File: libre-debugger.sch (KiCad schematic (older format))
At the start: 81 parts, among them J1 USB_C_Receptacle_USB2.0, J2 Conn_ST_STDC14, J4 Conn_01x16, Q1 2N7002, SW1 SW_SPDT, SW2 SW_Push, U1 FT2232H, U10 74LVC1G125, U11 74LVC1G125, U12 74LVC1G125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

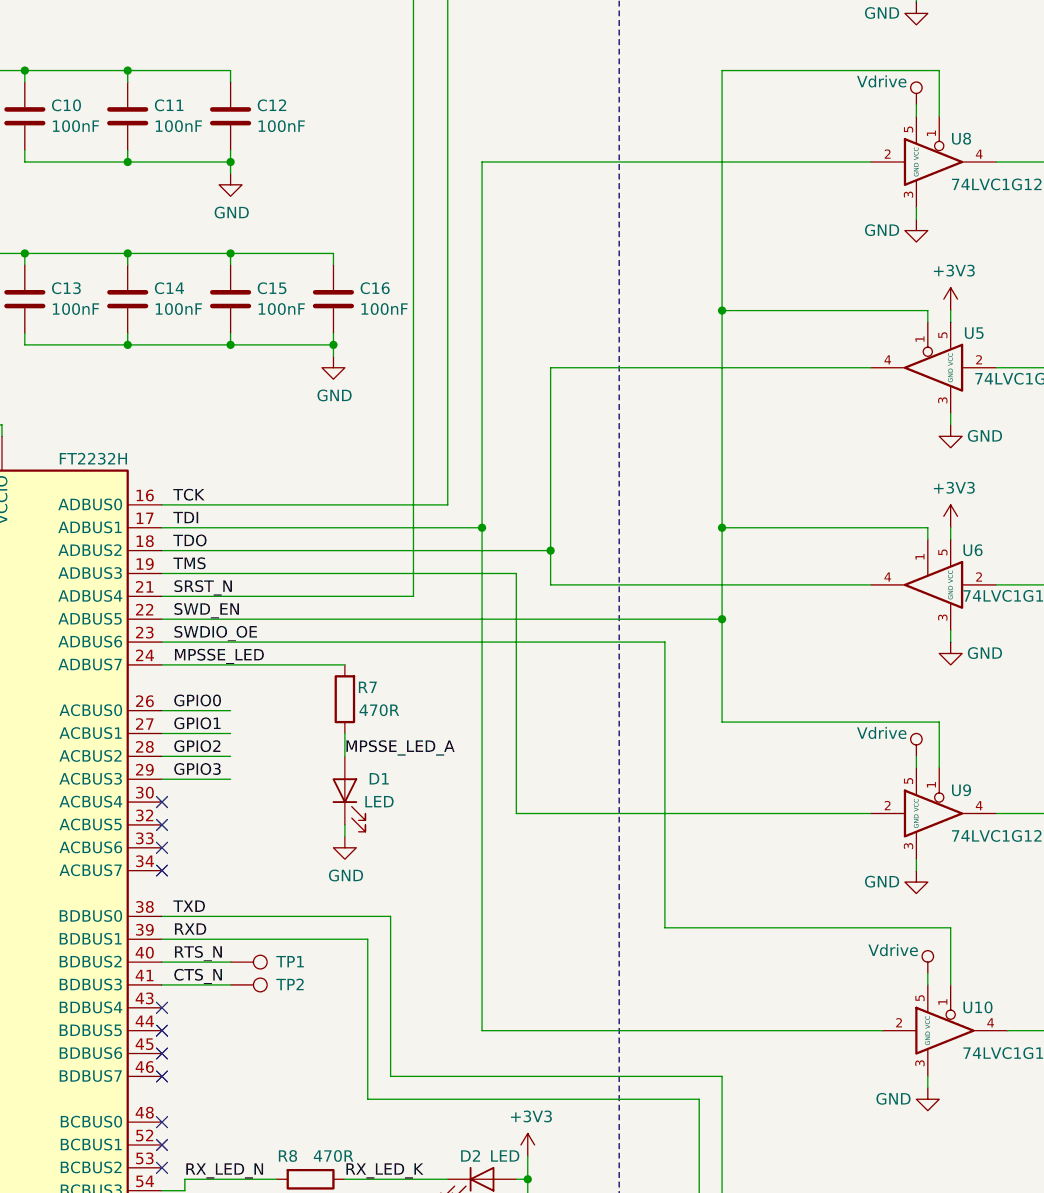
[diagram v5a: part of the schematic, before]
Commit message: Make MPSSE LED active low
So that all the activity LEDs have the same orientation.
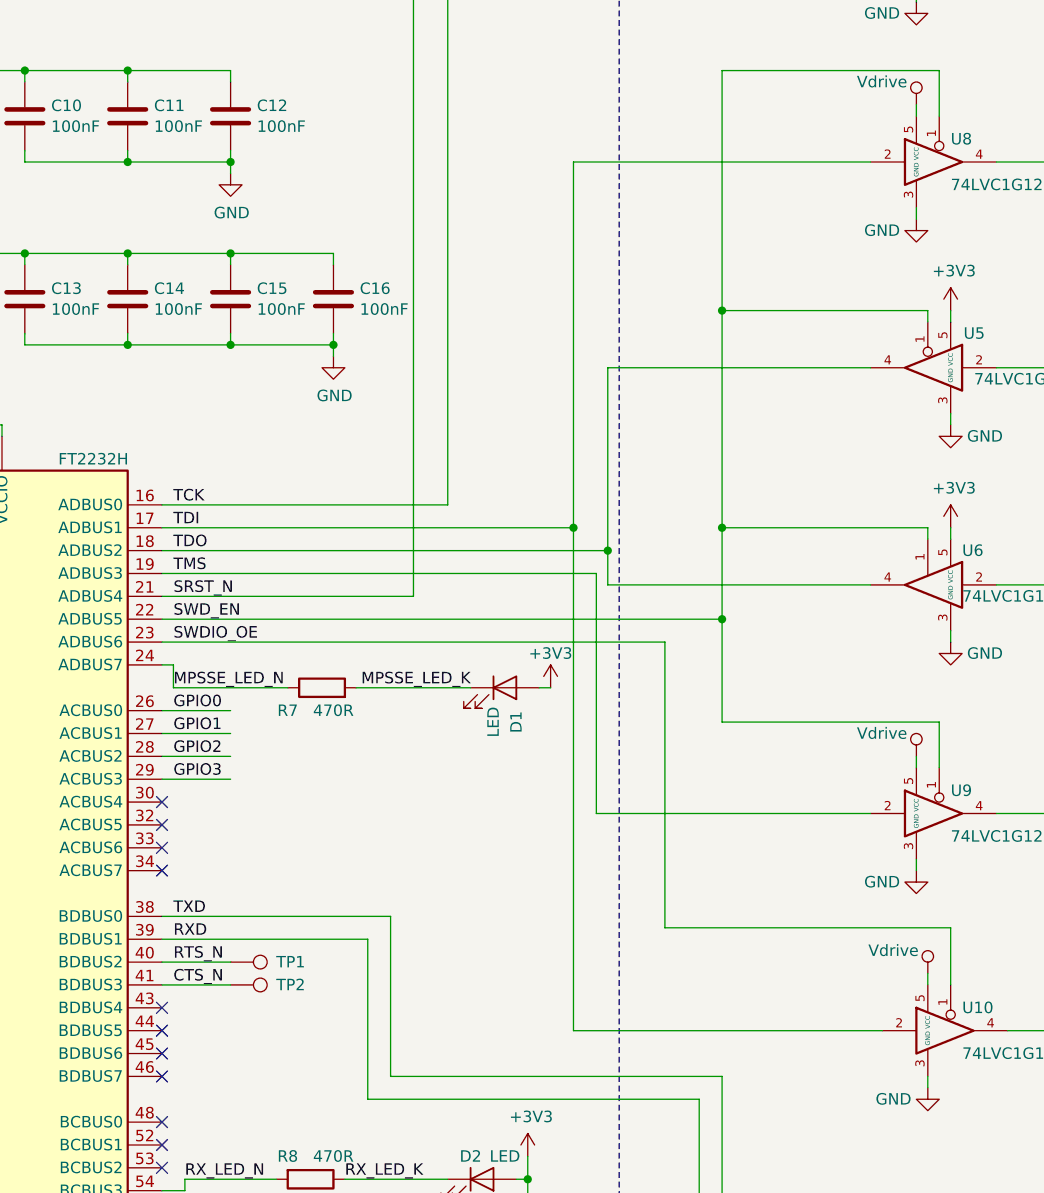
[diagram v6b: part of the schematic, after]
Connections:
- net labels added: MPSSE_LED_K, MPSSE_LED_N
- net labels removed: MPSSE_LED, MPSSE_LED_A
- wire segments 367 -> 369
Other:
- moved on the sheet: D1, R7
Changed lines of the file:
@@
 Text Notes 8850 7850 0    50   ~ 0
 ON only when USB configured
-Text Label 8450 4750 0    50   ~ 0
-MPSSE_LED
-$Comp
-L Device:LED D1
-U 1 1 5C62F385
-P 9200 5300
-F 0 "D1" V 9250 5150 50  0000 C CNN
-F 1 "LED" V 9150 5150 50  0000 C CNN
-F 2 "LED_SMD:LED_0603_1608Metric" H 9200 5300 50  0001 C CNN
-F 3 "~" H 9200 5300 50  0001 C CNN
-	1    9200 5300
-	0    -1   -1   0
-$EndComp
-Text Label 9200 5150 0    50   ~ 0
-MPSSE_LED_A
-Wire Wire Line
-	8400 4750 9200 4750
-$Comp
-L power:GND #PWR031
-U 1 1 5C6507DD
-P 9200 5500
-F 0 "#PWR031" H 9200 5250 50  0001 C CNN
-F 1 "GND" H 9205 5327 50  0000 C CNN
-F 2 "" H 9200 5500 50  0001 C CNN
-F 3 "" H 9200 5500 50  0001 C CNN
-	1    9200 5500
-	1    0    0    -1
-$EndComp
 Wire Wire Line
 	9650 4050 9650 1600
@@
 SWDIO_OE
 Wire Wire Line
-	8400 4150 9800 4150
-Wire Wire Line
-	9800 2550 9800 4150
+	8400 4150 10200 4150
+Wire Wire Line
+	10200 2550 10200 4150
 Wire Wire Line
 	9300 5950 9300 6650
@@
 Wire Wire Line
 	8400 4550 10850 4550
-$Comp
-L Device:R R7
-U 1 1 5C62F38F
-P 9200 4900
-F 0 "R7" H 9100 4850 50  0000 C CNN
-F 1 "470R" H 9050 4950 50  0000 C CNN
-F 2 "Resistor_SMD:R_0603_1608Metric" V 9130 4900 50  0001 C CNN
-F 3 "~" H 9200 4900 50  0001 C CNN
-	1    9200 4900
-	-1   0    0    1
-$EndComp
-Wire Wire Line
-	9200 5500 9200 5450
-Wire Wire Line
-	9200 5150 9200 5050
-Wire Wire Line
-	8400 4350 9950 4350
-Connection ~ 9800 4150
+Wire Wire Line
+	8400 4350 10300 4350
+Connection ~ 10200 4150
 Wire Wire Line
 	8400 4650 10600 4650
@@
 	9650 1600 11500 1600
 Wire Wire Line
-	9800 2550 11500 2550
+	10200 2550 11500 2550
 Wire Wire Line
 	11800 2150 10850 2150
@@
 $EndComp
 Wire Wire Line
-	11500 4400 10100 4400
-Wire Wire Line
-	10100 4400 10100 4250
-Wire Wire Line
 	13750 3000 13750 3450
 Wire Wire Line
@@
 	13650 4400 13650 2900
 Wire Wire Line
-	9950 5400 11500 5400
-Wire Wire Line
-	9950 4350 9950 5400
+	10300 5400 11500 5400
+Wire Wire Line
+	10300 4350 10300 5400
 Wire Wire Line
 	12050 5400 13650 5400
@@
 Connection ~ 13650 5400
 Wire Wire Line
-	9800 4150 9800 6350
+	10200 4150 10200 6350
 Wire Wire Line
 	10850 2150 10850 3200
@@
 	9400 5850 9400 6550
 Wire Wire Line
-	9800 6350 11550 6350
+	10200 6350 11550 6350
 Wire Wire Line
 	10600 4650 10600 5900
 Wire Wire Line
-	10100 3450 11500 3450
-Connection ~ 10100 4250
-Wire Wire Line
-	8400 4250 10100 4250
-Wire Wire Line
-	10100 3450 10100 4250
+	10350 3450 11500 3450
 Wire Notes Line
 	10400 600  13350 600
@@
 Wire Wire Line
 	5300 4650 5300 4600
+Wire Wire Line
+	10350 3450 10350 4250
+Wire Wire Line
+	8400 4250 10350 4250
+Connection ~ 10350 4250
+Wire Wire Line
+	10350 4400 10350 4250
+Wire Wire Line
+	11500 4400 10350 4400
+Text Label 8450 4850 0    50   ~ 0
+MPSSE_LED_N
+Wire Wire Line
+	8400 4750 8450 4750
+Wire Wire Line
+	8450 4850 8450 4750
+$Comp
+L Device:R R7
+U 1 1 5C62F38F
+P 9100 4850
+F 0 "R7" V 9000 5000 50  0000 C CNN
+F 1 "470R" V 9000 4800 50  0000 C CNN
+F 2 "Resistor_SMD:R_0603_1608Metric" V 9030 4850 50  0001 C CNN
+F 3 "~" H 9100 4850 50  0001 C CNN
+	1    9100 4850
+	0    -1   -1   0
+$EndComp
+Wire Wire Line
+	8950 4850 8450 4850
+$Comp
+L Device:LED D1
+U 1 1 5C62F385
+P 9900 4850
+F 0 "D1" V 9950 4700 50  0000 C CNN
+F 1 "LED" V 9850 4700 50  0000 C CNN
+F 2 "LED_SMD:LED_0603_1608Metric" H 9900 4850 50  0001 C CNN
+F 3 "~" H 9900 4850 50  0001 C CNN
+	1    9900 4850
+	1    0    0    -1
+$EndComp
+$Comp
+L power:+3V3 #PWR0108
+U 1 1 5DBB9689
+P 10100 4850
+F 0 "#PWR0108" H 10100 4700 50  0001 C CNN
+F 1 "+3V3" H 10100 5000 50  0000 C CNN
+F 2 "" H 10100 4850 50  0001 C CNN
+F 3 "" H 10100 4850 50  0001 C CNN
+	1    10100 4850
+	1    0    0    -1
+$EndComp
+Wire Wire Line
+	9250 4850 9750 4850
+Wire Wire Line
+	10050 4850 10100 4850
+Text Label 9750 4850 2    50   ~ 0
+MPSSE_LED_K
 $EndSCHEMATC

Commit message: Add pull up on SWDIO_OE and layout clean-up
- To prevent the buffer to be active when the FTDI pin is High-Z.
- Some cleanup including silkscreen and Fab
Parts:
- added R23: 10k, Resistor_SMD:R_0603_1608Metric, symbol Device:R
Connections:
- wire segments 369 -> 371
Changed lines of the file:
@@
 Text Label 9750 4850 2    50   ~ 0
 MPSSE_LED_K
+$Comp
+L Device:R R23
+U 1 1 5DBD9233
+P 8400 9500
+F 0 "R23" V 8300 9400 50  0000 C CNN
+F 1 "10k" V 8300 9600 50  0000 C CNN
+F 2 "Resistor_SMD:R_0603_1608Metric" V 8330 9500 50  0001 C CNN
+F 3 "~" H 8400 9500 50  0001 C CNN
+	1    8400 9500
+	-1   0    0    1
+$EndComp
+$Comp
+L power:+3V3 #PWR031
+U 1 1 5DBD97FD
+P 8400 9200
+F 0 "#PWR031" H 8400 9050 50  0001 C CNN
+F 1 "+3V3" H 8415 9373 50  0000 C CNN
+F 2 "" H 8400 9200 50  0001 C CNN
+F 3 "" H 8400 9200 50  0001 C CNN
+	1    8400 9200
+	1    0    0    -1
+$EndComp
+Wire Wire Line
+	8400 9650 8400 10200
+Text Label 8400 9750 3    50   ~ 0
+SWDIO_OE
+Wire Wire Line
+	8400 9200 8400 9350
 $EndSCHEMATC

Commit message: Add many MPNs and LCSC PNs
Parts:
- C10, C11, C12, C13, C14, C15, C16, C18, C19, C20, C21, C22, C8, C9: LCSC_PN (none) -> C14663; MPN (none) -> CC0603KRX7R9BB104; Manufacturer (none) -> Yageo
- C17, C5, C6, C7: LCSC_PN (none) -> C19666; MPN (none) -> CL10A475KO8NNNC; Manufacturer (none) -> Samsung Electro-Mechanics
- C3, C4: LCSC_PN (none) -> C1656; MPN (none) -> CL10C270JB8NNNC; Manufacturer (none) -> Samsung Electro-Mechanics
- D1, D2, D3, D4, D5, D6: LCSC_PN (none) -> C72043; MPN (none) -> 19-217/GHC-YR1S2/3T; Manufacturer (none) -> Everlight Elec
- Q1: LCSC_PN (none) -> C8545
- R1, R2: LCSC_PN (none) -> C23186
- R10, R18, R21, R7, R8, R9: LCSC_PN (none) -> C23179
- R11, R12, R13, R14, R15, R16, R19, R20: LCSC_PN (none) -> C22775
- R17, R23, R3, R6: LCSC_PN (none) -> C25804
- R4: LCSC_PN (none) -> C22790
- U1: LCSC_PN (none) -> C27882
- U10, U11, U12, U5, U7, U8, U9: LCSC_PN (none) -> C12519; MPN (none) -> 74LVC1G125GW,125; Manufacturer (none) -> Nexperia
- U2: LCSC_PN (none) -> C88419; MPN (none) -> MIC5504-3.3YM5-TR; Manufacturer (none) -> Microchip
- U3: LCSC_PN (none) -> C85364
- U6: LCSC_PN (none) -> C55052; MPN (none) -> 74LVC1G126GW,125; Manufacturer (none) -> Nexperia
- Y1: LCSC_PN (none) -> C9002; MPN (none) -> X322512MSB4SI; Manufacturer (none) -> Yangxing Tech
